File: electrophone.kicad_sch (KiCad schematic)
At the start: 18 parts, among them J1 AudioJack3, J2 Conn_01x02_Female, Q1 2N7000, Q2 2N7000

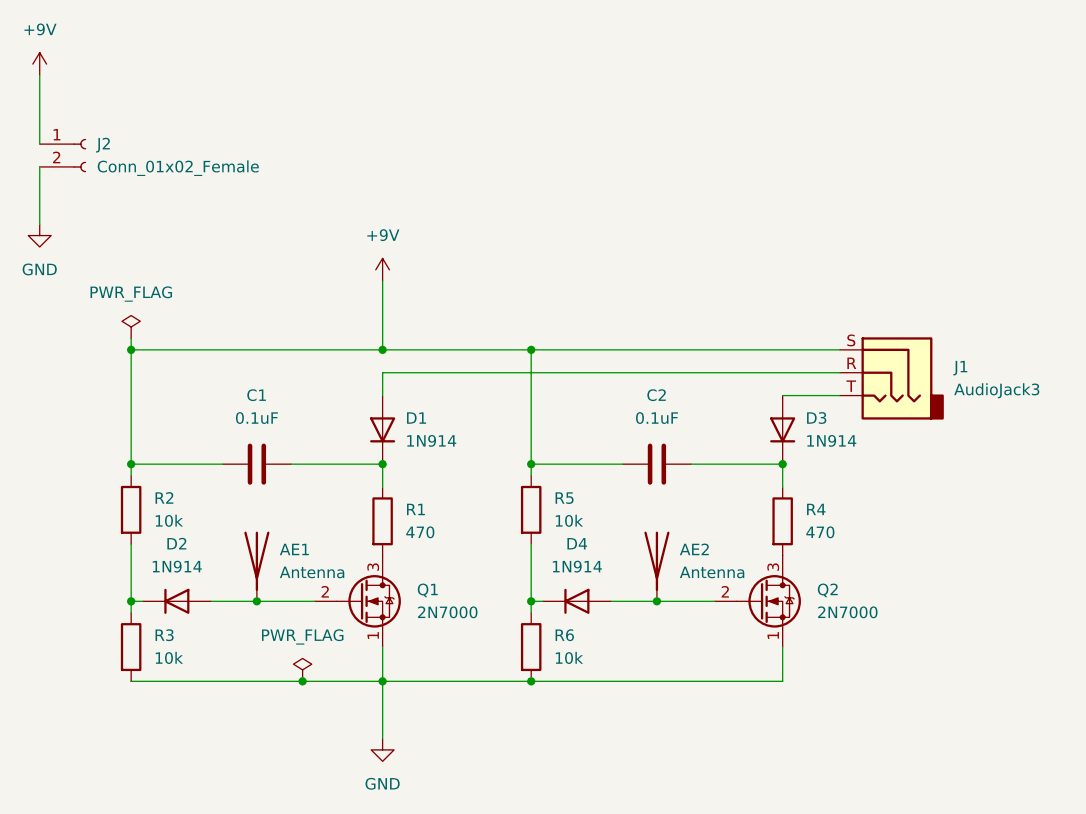
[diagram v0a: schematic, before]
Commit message: Move capacitors to where they belong
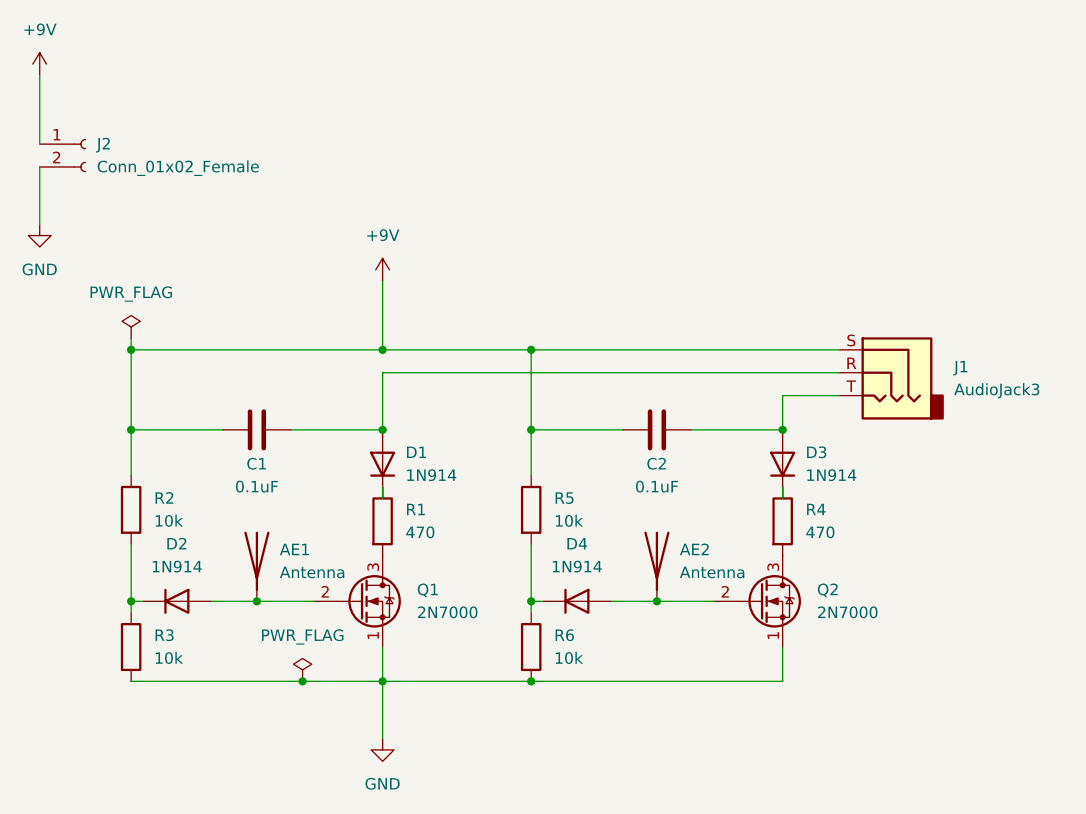
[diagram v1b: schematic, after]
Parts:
- J1: footprint (none) -> Connector_Audio:Jack_3.5mm_Lumberg_1503_07_Horizontal
- J2: footprint (none) -> Connector_Wire:SolderWire-0.75sqmm_1x02_P4.8mm_D1.25mm_OD2.3mm_Relief2x
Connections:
- net at D3.1 (K), R4.1: no longer C2.2
- net at D1.1 (K), R1.1: no longer C1.2
- net at D1.2 (A), J1.R: now also C1.2
- net at D3.2 (A), J1.T: now also C2.2
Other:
- moved on the sheet: C1, C2, D1, D3

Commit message: Contrary to what you might think... too much gain is bad!
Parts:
- R1, R4: value 470 -> 10k
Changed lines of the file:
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@@
       (effects (font (size 1.27 1.27)) (justify left))
     )
-    (property "Value" "470" (id 1) (at 194.31 83.8199 0)
+    (property "Value" "10k" (id 1) (at 194.31 83.8199 0)
       (effects (font (size 1.27 1.27)) (justify left))
     )
@@
       (effects (font (size 1.27 1.27)) (justify left))
     )
-    (property "Value" "470" (id 1) (at 149.86 83.8199 0)
+    (property "Value" "10k" (id 1) (at 149.86 83.8199 0)
       (effects (font (size 1.27 1.27)) (justify left))
     )
@@
     )
     (path "/1b404d6d-a18c-4ba9-a0dd-27042b6bd762"
-      (reference "R1") (unit 1) (value "470") (footprint "Resistor_THT:R_Axial_DIN0207_L6.3mm_D2.5mm_P10.16mm_Horizontal")
+      (reference "R1") (unit 1) (value "10k") (footprint "Resistor_THT:R_Axial_DIN0207_L6.3mm_D2.5mm_P10.16mm_Horizontal")
     )
     (path "/8b29aad6-dcd5-46c3-b16e-9c54262500bc"
@@
     )
     (path "/1a17eedb-072f-466d-875c-a1065a4614f1"
-      (reference "R4") (unit 1) (value "470") (footprint "Resistor_THT:R_Axial_DIN0207_L6.3mm_D2.5mm_P10.16mm_Horizontal")
+      (reference "R4") (unit 1) (value "10k") (footprint "Resistor_THT:R_Axial_DIN0207_L6.3mm_D2.5mm_P10.16mm_Horizontal")
     )
     (path "/106a0959-b48c-4636-bb87-8a38e97edc32"
